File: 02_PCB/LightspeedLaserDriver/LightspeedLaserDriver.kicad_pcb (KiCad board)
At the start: 2 copper layers, 50 x 30 mm, 46 parts, among them IC1 LT8365JMSE, J1 Conn_01x02_Pin, J2 SMA, J3 Conn_01x02_Pin, J4 SMA, Q1 FMMT417TD, SW1 SW_SPDT

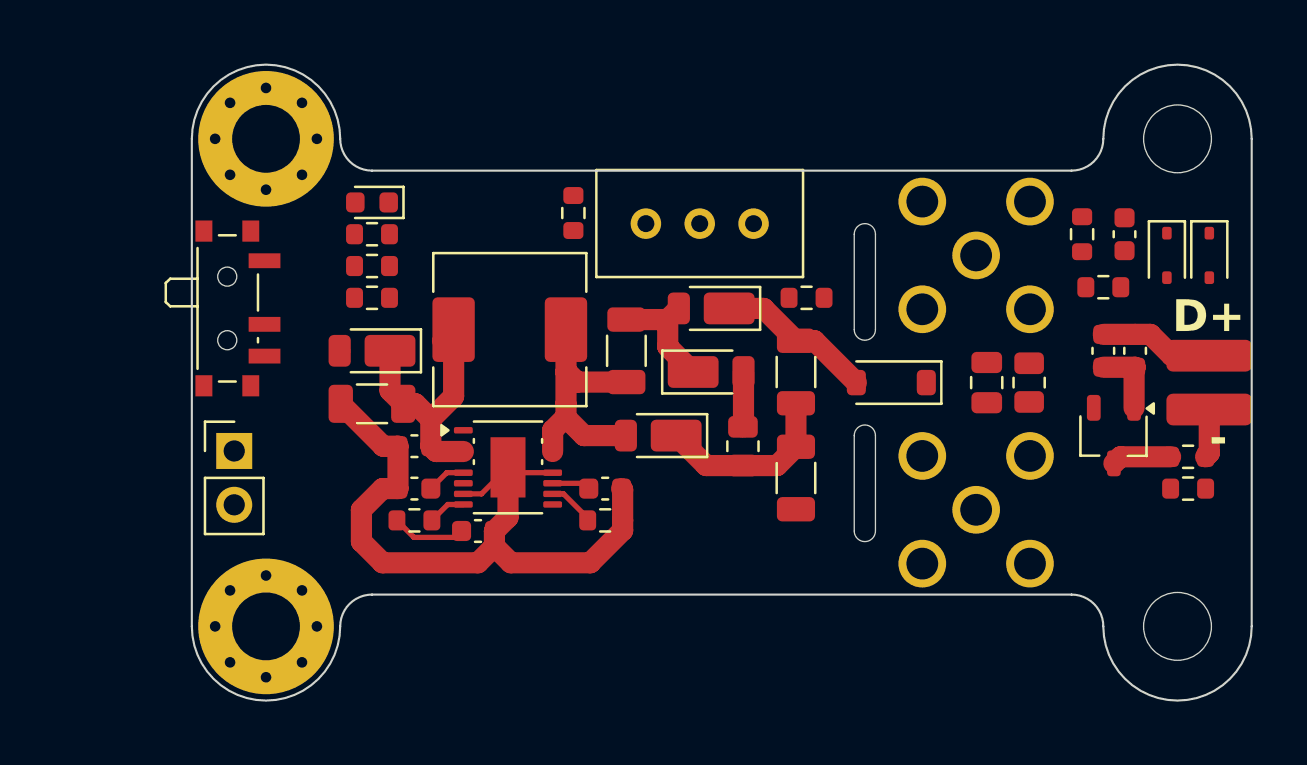
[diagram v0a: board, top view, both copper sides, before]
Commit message: feat(pcb): add peripherals to PCB
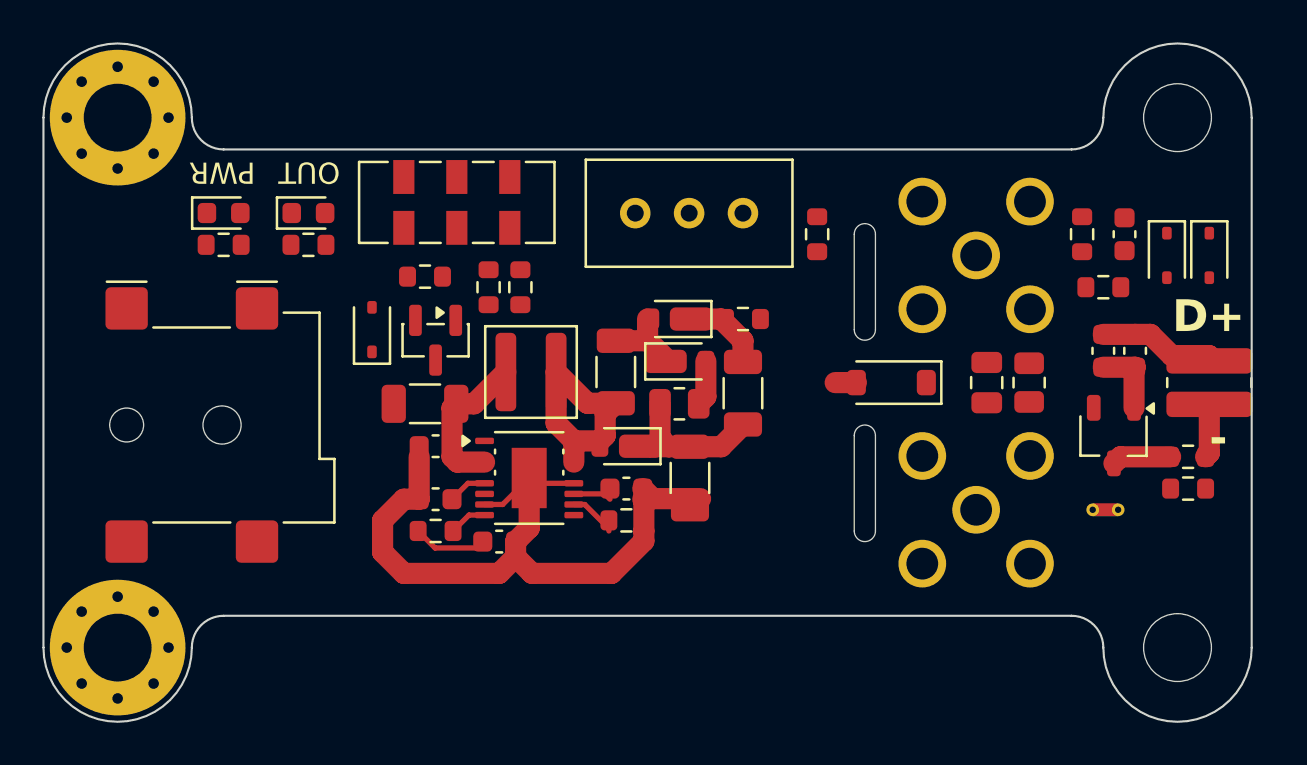
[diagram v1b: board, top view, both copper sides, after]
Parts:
- removed J1: Conn_01x02_Pin, Connector_PinHeader_2.54mm:PinHeader_1x02_P2.54mm_Vertical
- removed SW1: SW_SPDT, Button_Switch_SMD:SW_SPDT_PCM12
- added D9: SZMM3Z10VT1G, Diode_SMD:D_SOD-323, F.Cu at (118.5, 107.5)
- added J5: Barrel_Jack_Switch, Connector_BarrelJack:BarrelJack_Wuerth_694106106102_2.0x5.5mm, F.Cu at (110.0, 112.0)
- added NT1: NetTie_2, NetTie:NetTie-2_THT_Pad0.3mm, F.Cu at (153.7, 116.0)
- added Q2: PJA3463, Package_TO_SOT_SMD:SOT-23, F.Cu at (121.5, 108.0)
- added R14: 47k, Resistor_SMD:R_0603_1608Metric, F.Cu at (111.5, 103.5)
- added R15: 100k, Resistor_SMD:R_0603_1608Metric, F.Cu at (121.0, 105.0)
- added SW2: JS202011JAQN, Button_Switch_SMD:SW_DPDT_CK_JS202011JCQN, F.Cu at (122.5, 101.5)
- D1: value DFLS1150 -> LED; footprint Diode_SMD:D_PowerDI-123 -> LED_SMD:LED_0603_1608Metric
- D2, D3, D4: value DFLS1150 -> SMD115PBQ-TP; footprint Diode_SMD:D_PowerDI-123 -> CustomFootprints:D_SOD-323HE
- L1: value 10u -> 74438356220; footprint Inductor_SMD:L_Wuerth_HCM-7050 -> Inductor_SMD:L_Wuerth_MAPI-4020
- moved R5 11.5 mm to (139.5, 103.0)
- moved D1 9.55 mm to (111.5, 102.0), turned to 0 degrees
- moved H1 7.07 mm to (106.5, 97.5)
- moved H2 7.07 mm to (106.5, 122.5)
- moved R7 7.02 mm to (125.5, 105.5), turned to 90 degrees
- moved R8 5.59 mm to (124.0, 105.5), turned to -90 degrees
- moved C8 5.00 mm to (133.5, 114.5)
- moved RV1 4.61 mm to (136.0, 102.0), turned to 0 degrees
- moved R3 3.61 mm to (133.0, 111.0), turned to 180 degrees
- moved R4 3.16 mm to (136.0, 107.0)
- moved D5 3.04 mm to (115.5, 102.0), turned to 0 degrees
- moved R6 3.04 mm to (115.5, 103.5)
- moved C7 2.69 mm to (136.0, 110.5)
- moved C1 2.50 mm to (121.0, 111.0)
- moved L1 2.24 mm to (126.0, 109.5)
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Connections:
- D1 pad 1: /Boost Converter/VIN -> GND
- D5 pad 1: Net-(D5-K) -> GND
- R6 pad 1: /Boost Converter/VIN -> Net-(R6-Pad1)
- R7 pad 2: /Boost Converter/VIN -> Net-(R6-Pad1)
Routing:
- net /Boost Converter/VIN: track 12.7 -> 7.18 mm
- net /Boost Converter/HV_OUT: track 7.45 -> 5.02 mm
- net Net-(D3-K): track 5.66 -> 3.94 mm
- net Net-(D2-K): track 8.65 -> 7.08 mm
- net GND: track 36.8 -> 36.2 mm
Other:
- board size 50 x 30 mm -> 57 x 32 mm
- board text added: "OUT"
- board text added: "PWR"

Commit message: feat(pcb): route all traces
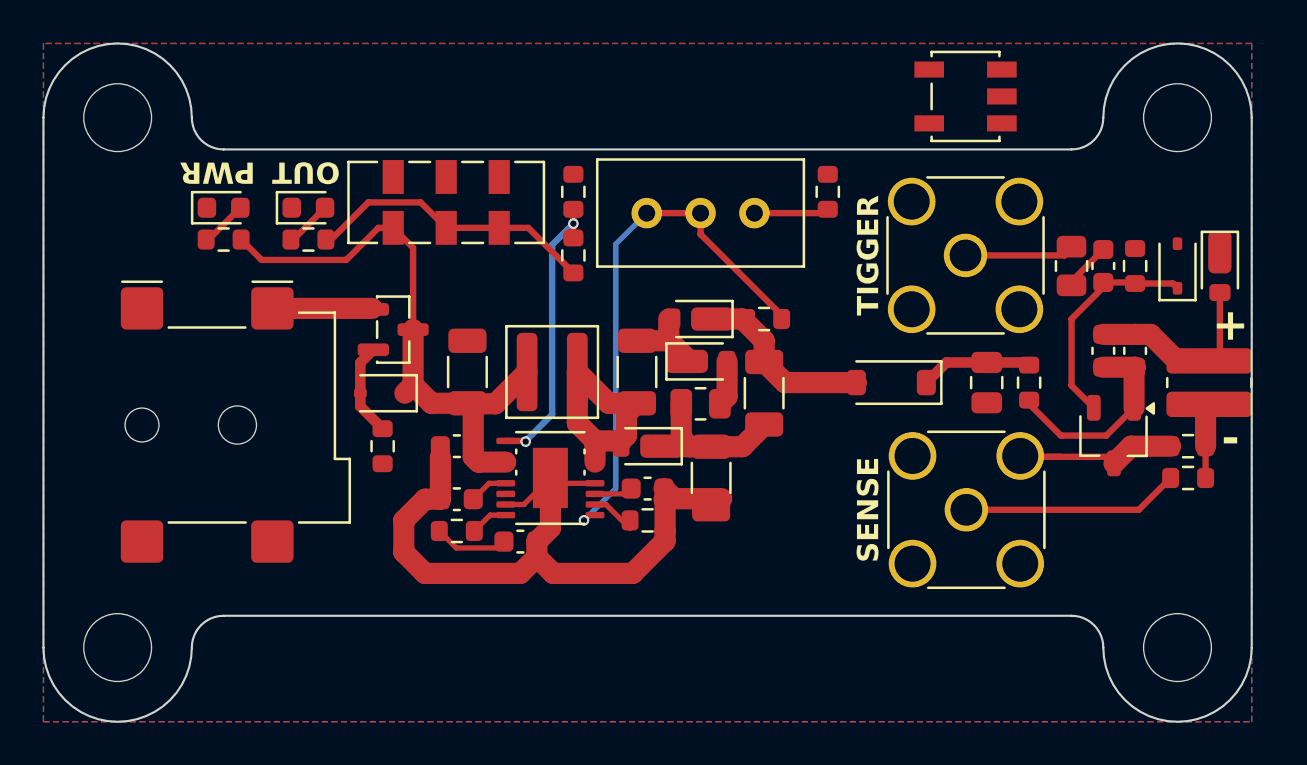
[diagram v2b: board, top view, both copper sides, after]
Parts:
- added TR1: MABAES0060, Transformer_SMD:Transformer_MACOM_SM-22, F.Cu at (146.5, 96.5)
- D9: renamed from D8; value SD103AWS -> SMD115PBQ-TP; footprint Diode_SMD:D_SOD-323 -> CustomFootprints:D_SOD-323HE
- H1, H2: value MountingHole_Pad -> MountingHole; footprint MountingHole:MountingHole_3.2mm_M3_Pad_Via -> MountingHole:MountingHole_3.2mm_M3
- J2, J4: footprint Connector_Coaxial:SMA_Molex_73251-2200_Horizontal -> Connector_Coaxial:SMA_Wurth_60312002114503_Vertical; moved to F.Cu
- R11: renamed from R9; value 1k;1% -> 50R;1%; footprint Resistor_SMD:R_0805_2012Metric -> Resistor_SMD:R_0603_1608Metric
- R12: renamed from R10; value 50R;1% -> 1k;1%; footprint Resistor_SMD:R_0603_1608Metric -> Resistor_SMD:R_0805_2012Metric
- moved R1 8.25 mm to (119.0, 113.0), turned to -90 degrees
- moved R10 6.02 mm to (128.0, 101.0)
- moved RV1 4.54 mm to (131.5, 102.0), turned to 180 degrees
- moved NT1 3.68 mm to (151.0, 113.5)
- moved D1 3.04 mm to (119.0, 110.5), turned to 180 degrees
- moved R9 2.92 mm to (128.0, 104.0), turned to -90 degrees
- moved C1 2.50 mm to (123.0, 109.5), turned to -90 degrees
- moved Q1 2.06 mm to (119.5, 107.5), turned to 0 degrees
- moved R7 2.06 mm to (140.0, 101.0), turned to 90 degrees
- moved C10 1.80 mm to (153.0, 104.5)
- moved R13 1.80 mm to (154.5, 104.5), turned to -90 degrees
- moved R12 1.58 mm to (151.5, 104.5), turned to -90 degrees
- moved C2 1.00 mm to (122.5, 113.0)
- moved C3 1.00 mm to (122.5, 115.5)
- moved C4 1.00 mm to (125.5, 117.5)
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- renumbered D9 to D1, D1 to D2, D2 to D3, D3 to D4, D4 to D5, D5 to D6, D6 to D7, D7 to D8, J5 to J1, Q2 to Q1, Q1 to Q2, R15 to R1, R8 to R10, R11 to R13, R12 to R14, R13 to R15, R14 to R2, R1 to R3, R2 to R4, R3 to R5, R4 to R6, R5 to R7, R6 to R8, R7 to R9, SW2 to SW1
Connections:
- C10 pad 2: Net-(D7-K) -> /Driver Stage/TRIG
- C11 pad 1: Net-(Q1-C) -> Net-(Q2-C)
- C12 pad 1: Net-(Q1-C) -> Net-(Q2-C)
- C9 pad 1: Net-(D6-K) -> Net-(D7-K)
- D7 pad 1: Net-(D6-K) -> Net-(D7-K)
- D8 pad 1: Net-(D7-K) -> /Driver Stage/TRIG
- D8 pad 2: GND -> Net-(D8-A)
- J2 pad 1: /Driver Stage/TRIG -> /Driver Stage/TRIG_IN_+
- J2 pad 2: GND -> /Driver Stage/TRIG_IN-
- Q2 pad 1: Net-(Q1-C) -> Net-(Q2-C)
- Q2 pad 2: Net-(D7-K) -> /Driver Stage/TRIG
- R11 pad 1: Net-(D6-K) -> Net-(R11-Pad1)
- R11 pad 2: Net-(Q1-C) -> Net-(C10-Pad1)
- R12 pad 1: /Driver Stage/TRIG -> Net-(D7-K)
- R12 pad 2: Net-(C10-Pad1) -> Net-(Q2-C)
- R13 pad 1: GND -> Net-(D8-A)
- R13 pad 2: Net-(D7-K) -> /Driver Stage/TRIG
- R7 pad 1: Net-(R5-Pad1) -> Net-(R7-Pad1)
- R8 pad 1: Net-(R6-Pad1) -> Net-(R8-Pad1)
- R9 pad 2: Net-(R6-Pad1) -> Net-(R8-Pad1)
- RV1 pad 1: Net-(R5-Pad1) -> /Boost Converter/FBX
- RV1 pad 3: /Boost Converter/FBX -> Net-(R7-Pad1)
- SW1 pad 1: unconnected-(SW2-A-Pad1) -> Net-(R8-Pad1)
- SW1 pad 2: Net-(R6-Pad1) -> Net-(R8-Pad1)
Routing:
- net /Boost Converter/FBX: track 0.00 -> 25.5 mm, vias 0 -> 1
- net /Boost Converter/VIN: track 7.18 -> 26.7 mm
- net /Driver Stage/TRIG: track 0.00 -> 16.2 mm
- net Net-(R8-Pad1): track 0.00 -> 13.9 mm
- net /Boost Converter/EN: track 0.00 -> 13.5 mm, vias 0 -> 2
- net /Driver Stage/I_sense+: track 0.00 -> 10.8 mm
- net Net-(Q2-C): track 0.00 -> 9.64 mm
- net Net-(D7-K): track 0.00 -> 5.26 mm
- net Net-(Q1-D): track 0.00 -> 4.71 mm
- net Net-(D1-A): track 0.00 -> 4.41 mm
- net GND: track 36.2 -> 40.1 mm
- net /Boost Converter/HV_OUT: track 5.02 -> 8.78 mm
- net Net-(R7-Pad1): track 0.00 -> 3.53 mm
- net Net-(Q1-C): track 3.44 -> 0.00 mm
- net Net-(D6-A): track 0.00 -> 2.23 mm
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- added copper zone on B.Cu, net GND
- added copper zone on F.Cu, net GND
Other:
- outline, holes or cut-outs redrawn
- board text added: "+"
- board text added: "SENSE"
- board text added: "TIGGER"
- board text removed: "D+"

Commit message: feat(pcb): laser driver layout draft finished, add high voltage indicator LED and discharge path
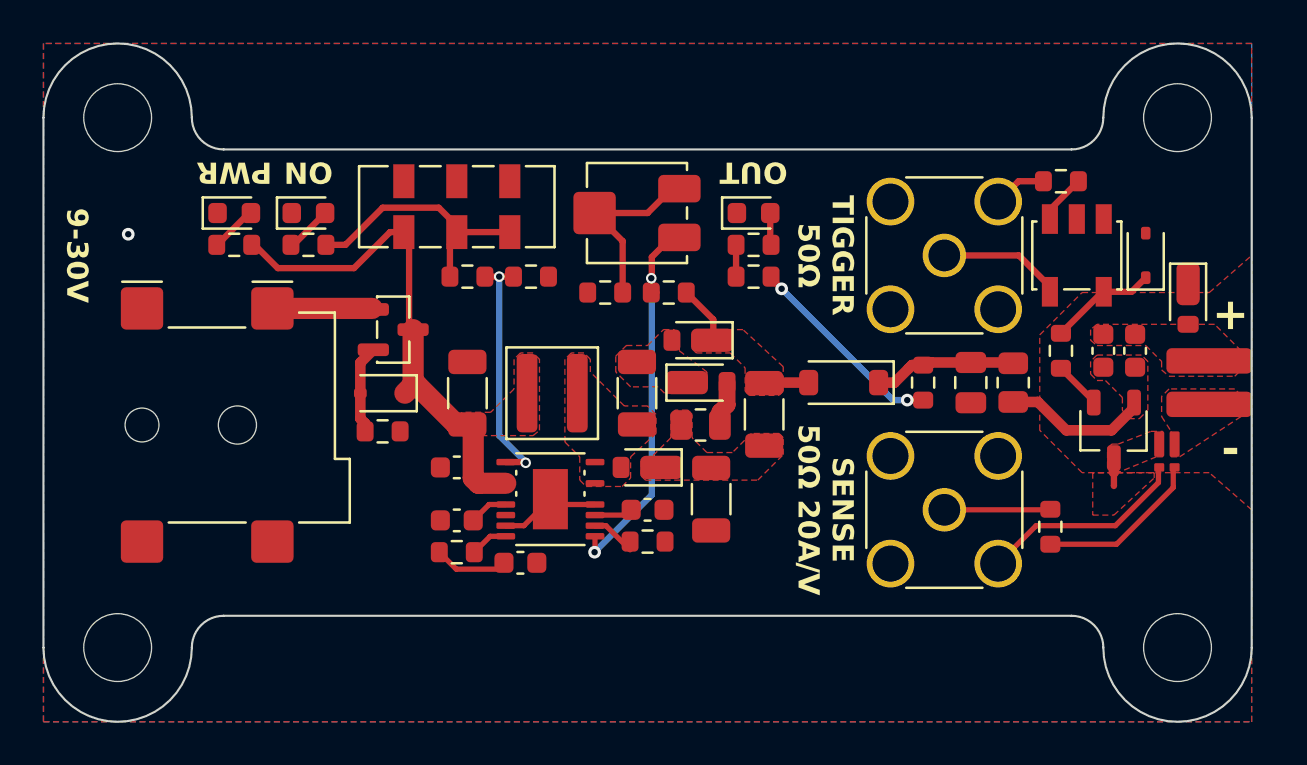
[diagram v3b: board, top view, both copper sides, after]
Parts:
- removed C10: 10nF;100V, Capacitor_SMD:C_0603_1608Metric
- removed R14: 0.1;1%, Resistor_SMD:R_0603_1608Metric
- added D10: LED, LED_SMD:LED_0603_1608Metric, F.Cu at (136.5, 102.0)
- added R16: 160k;1%, Resistor_SMD:R_0603_1608Metric, F.Cu at (136.5, 103.5)
- added R17: 160;1%, Resistor_SMD:R_0603_1608Metric, F.Cu at (136.5, 105.0)
- added R18: 160k;1%, Resistor_SMD:R_0603_1608Metric, F.Cu at (144.5, 110.0)
- added R19: 20m;1%, CustomFootprints:FC4L16, F.Cu at (156.0, 113.2)
- R12: value 1k;1% -> 2k;1%
- R13: value 100k;1% -> 50;1%
- RV1: footprint Potentiometer_THT:Potentiometer_Bourns_3296W_Vertical -> Potentiometer_SMD:Potentiometer_Bourns_3314J_Vertical
- moved R7 11.5 mm to (129.5, 105.8), turned to 180 degrees
- moved TR1 9.15 mm to (151.8, 104.0), turned to 90 degrees
- moved R15 6.89 mm to (150.5, 116.8), turned to 90 degrees
- moved R12 6.15 mm to (148.8, 110.0)
- moved R13 5.32 mm to (151.0, 100.5), turned to 180 degrees
- moved R9 5.10 mm to (123.0, 105.0), turned to 180 degrees
- moved R6 4.67 mm to (132.5, 105.8), turned to 0 degrees
- moved R10 4.47 mm to (126.0, 105.0), turned to 180 degrees
- moved NT1 2.85 mm to (153.5, 114.9), turned to 90 degrees
- moved D7 2.25 mm to (140.8, 110.0)
- moved D9 2.12 mm to (157.0, 106.0)
- moved R11 2.12 mm to (151.0, 108.5)
- moved D8 1.58 mm to (155.0, 104.0)
- moved J4 1.04 mm to (145.5, 116.0)
- moved C1 1.00 mm to (123.0, 110.5)
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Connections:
- net Net-(D3-A) renamed /Boost Converter/BOOST_NODE1
- net Net-(D3-K) renamed /Boost Converter/BOOST_NODE3
- net Net-(D4-K) renamed /Boost Converter/BOOST_NODE2
- net Net-(D7-K) renamed /Driver Stage/HV_DRIVER
- net Net-(Q2-C) renamed /Driver Stage/DRIVER_CAPS
- D8 pad 1: /Driver Stage/TRIG -> Net-(D8-K)
- D8 pad 2: Net-(D8-A) -> GND
- NT1 pad 2: /Driver Stage/I_sense- -> /Driver Stage/DRV_GND
- Q2 pad 3: GND -> /Driver Stage/DRV_GND
- R11 pad 1: Net-(R11-Pad1) -> Net-(D8-K)
- R11 pad 2: Net-(C10-Pad1) -> /Driver Stage/TRIG
- R13 pad 1: Net-(D8-A) -> Net-(R13-Pad1)
- R13 pad 2: /Driver Stage/TRIG -> /Driver Stage/TRIG_IN-
- R15 pad 1: /Driver Stage/D- -> Net-(R15-Pad1)
- RV1 pad 2: /Boost Converter/FBX -> Net-(R7-Pad1)
- TR1 pad 1: /Driver Stage/TRIG_IN- -> /Driver Stage/TRIG_IN_+
- TR1 pad 2: Net-(D8-A) -> Net-(D8-K)
- TR1 pad 3: Net-(R11-Pad1) -> GND
- TR1 pad 5: /Driver Stage/TRIG_IN_+ -> Net-(R13-Pad1)
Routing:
- net GND: track 40.1 -> 4.48 mm, vias 0 -> 1
- net /Driver Stage/TRIG: track 16.2 -> 2.19 mm
- net /Boost Converter/BOOST_NODE1: track 11.8 -> 0.00 mm
- net Net-(R17-Pad1): track 0.00 -> 9.56 mm, vias 0 -> 2
- net /Driver Stage/D+: track 8.95 -> 0.00 mm
- net /Driver Stage/I_sense-: track 0.98 -> 9.88 mm
- net Net-(R15-Pad1): track 0.00 -> 7.88 mm
- net /Boost Converter/BOOST_NODE3: track 7.08 -> 0.00 mm
- net /Boost Converter/FBX: track 25.5 -> 18.5 mm, vias 1 -> 2
- net /Driver Stage/TRIG_IN_+: track 0.00 -> 5.84 mm
- net /Driver Stage/I_sense+: track 10.8 -> 5.01 mm
- net Net-(R7-Pad1): track 3.53 -> 8.78 mm
- net Net-(D8-K): track 0.00 -> 5.09 mm
- net /Boost Converter/HV_OUT: track 8.78 -> 3.92 mm
- net /Boost Converter/BOOST_NODE2: track 3.94 -> 0.00 mm
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- added copper zone on F.Cu, net /Boost Converter/BOOST_NODE1
- added copper zone on F.Cu, net /Boost Converter/BOOST_NODE2
- added copper zone on F.Cu, net /Boost Converter/BOOST_NODE3
- added copper zone on F.Cu, net /Boost Converter/HV_OUT
- added copper zone on F.Cu, net /Boost Converter/VIN
- added copper zone on F.Cu, net /Driver Stage/D+
- added copper zone on F.Cu, net /Driver Stage/D-
- added copper zone on F.Cu, net /Driver Stage/DRIVER_CAPS
- added copper zone on F.Cu, net /Driver Stage/DRV_GND
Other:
- board text added: "9-30V"
- board text added: "Fixed Pulsewidth Avalanche Laser Driver Output is adjustable between 100-260V (c) Hannes Duske 2026 V0.1"
- board text added: "ON"
- board text added: "SENSE 50Ω 20A/V"
- board text added: "TIGGER 50Ω"
- board text added: "⚠︎ DANGER ⚠︎ HIGH VOLTAGE LASER RADIATION"
- board text removed: "SENSE"
- board text removed: "TIGGER"

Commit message: feat(pcb): improve the design draft
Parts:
- added F1: MFU0603FF03000, Fuse:Fuse_0603_1608Metric, F.Cu at (116.8, 105.8)
- added R14: 2k;1%, Resistor_SMD:R_0805_2012Metric, F.Cu at (155.0, 105.0)
- added R20: 100k;1%, Resistor_SMD:R_0603_1608Metric, F.Cu at (150.4, 111.7)
- C11, C12: value 100pF;500V -> 100p;500V
- C2: value 100u;100V -> 100n;100V
- C4: value 1nF;16V -> 1n;16V
- C7: value 220nF;200V -> 220n;200V
- C8: value 200nF;200V -> 220n;200V
- D10: value LED -> APTD1608LSURCK
- D2, D6: value LED -> APTD1608LCGCK
- J1: value Barrel_Jack_Switch -> 694106106102
- L1: value 74438356220 -> 7443732448100; footprint Inductor_SMD:L_Wuerth_MAPI-4020 -> Inductor_SMD_Wurth:L_Wurth_WE-LQSH-4020
- Q1: value PJA3463 -> PJA3463_R1_00001
- R11: value 50R;1% -> 50;1%
- R17: value 160;1% -> 160k;1%
- R19: value 20m;1% -> FC4L16R020FER
- R8: value 47k -> 47k;1%
- RV1: value 10k -> 3314J-1-103G
- moved D8 7.68 mm to (150.2, 110.0), turned to 180 degrees
- moved D7 3.26 mm to (138.1, 108.1)
- moved C2 2.70 mm to (124.8, 112.5), turned to 180 degrees
- moved C9 2.15 mm to (144.6, 110.0)
- moved R12 2.15 mm to (146.6, 110.0)
- moved R18 1.65 mm to (142.8, 110.0)
- moved NT1 1.26 mm to (154.7, 114.5)
- moved C1 1.01 mm to (123.2, 109.5)
- moved L1 1.00 mm to (127.1, 109.5)
- moved C3 0.70 mm to (122.5, 115.8)
- moved R11 0.61 mm to (150.4, 108.4), turned to 180 degrees
- moved R3 0.60 mm to (122.5, 117.4)
- moved Q1 0.50 mm to (120.0, 107.5)
- moved D1 0.50 mm to (119.5, 110.5)
- moved J1 0.50 mm to (110.7, 112.5)
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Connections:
- D8 pad 1: Net-(D8-K) -> /Driver Stage/TRIG
- D9 pad 1: GND -> Net-(D9-K)
- J1 pad 1: Net-(Q1-D) -> Net-(F1-Pad1)
- Q2 pad 1: /Driver Stage/DRIVER_CAPS -> /Driver Stage/TRIG
- Q2 pad 2: /Driver Stage/TRIG -> /Driver Stage/DRV_GND
- Q2 pad 3: /Driver Stage/DRV_GND -> /Driver Stage/DRIVER_CAPS
- R11 pad 1: Net-(D8-K) -> Net-(R11-Pad1)
- SW1 pad 1: Net-(R8-Pad1) -> GND
- TR1 pad 2: Net-(D8-K) -> Net-(R11-Pad1)
- TR1 pad 4: unconnected-(TR1-MP-Pad4) -> GND
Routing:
- net /Driver Stage/DRV_GND: track 0.66 -> 9.24 mm, vias 0 -> 2
- net /Boost Converter/VIN: track 23.1 -> 30.0 mm
- net Net-(D8-K): track 5.09 -> 0.00 mm
- net /Driver Stage/TRIG: track 2.19 -> 6.18 mm
- net Net-(R11-Pad1): track 0.00 -> 3.62 mm
- net Net-(R8-Pad1): track 12.3 -> 8.88 mm
- net Net-(Q1-D): track 4.71 -> 1.89 mm
- net Net-(F1-Pad1): track 0.00 -> 2.53 mm
- net Net-(D9-K): track 0.00 -> 2.23 mm
- net /Boost Converter/FBX: track 18.5 -> 17.2 mm
- net /Boost Converter/HV_OUT: track 3.92 -> 2.73 mm
- net Net-(R17-Pad1): track 9.56 -> 8.38 mm
- net Net-(C4-Pad2): track 3.08 -> 3.86 mm
- net /Driver Stage/DRIVER_CAPS: track 6.94 -> 7.31 mm, vias 0 -> 2
- net GND: vias 1 -> 47
- removed copper zone on F.Cu, net /Boost Converter/VIN
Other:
- board text added: "SENSE 20A/V 50Ω"
- board text removed: "SENSE 50Ω 20A/V"
